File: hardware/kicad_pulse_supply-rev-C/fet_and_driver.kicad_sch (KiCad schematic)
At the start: 52 parts, among them J2 SIG_EXT, Q1 GAN7R0-150LBE, U1 UCC27611DRVT, U4 MAX4378, U6 MCP1703T-5002E/MB

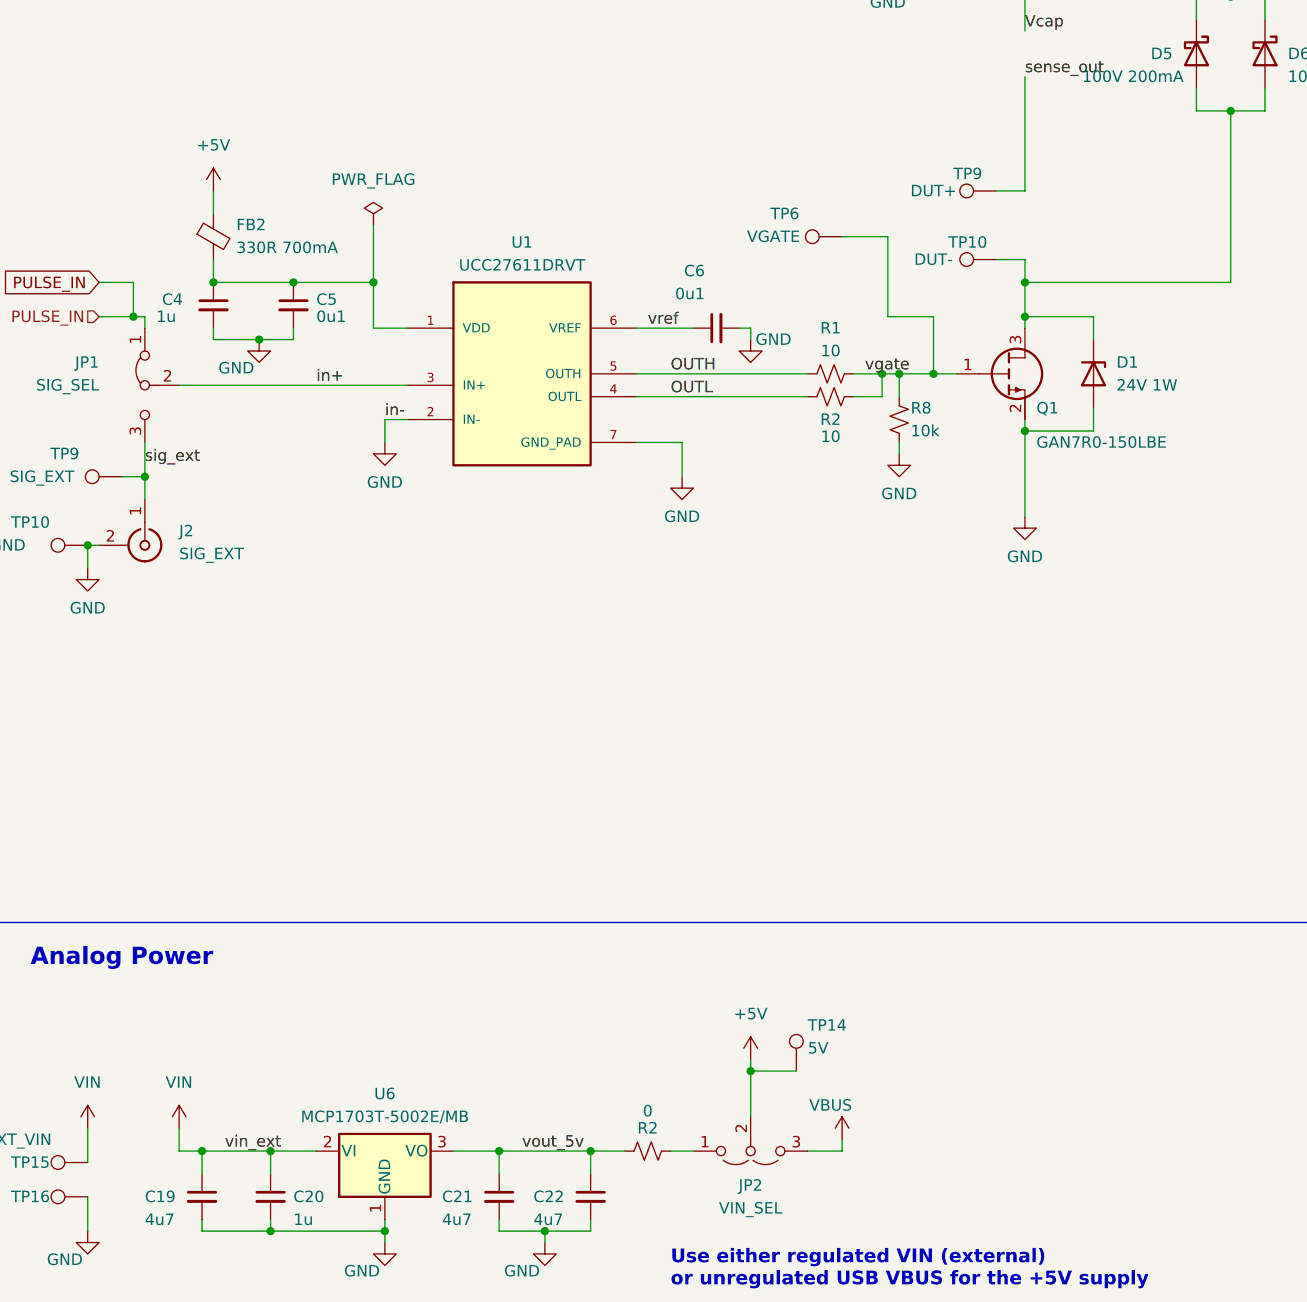
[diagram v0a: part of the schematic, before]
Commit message: Refactored main loop to use Arduino Strings
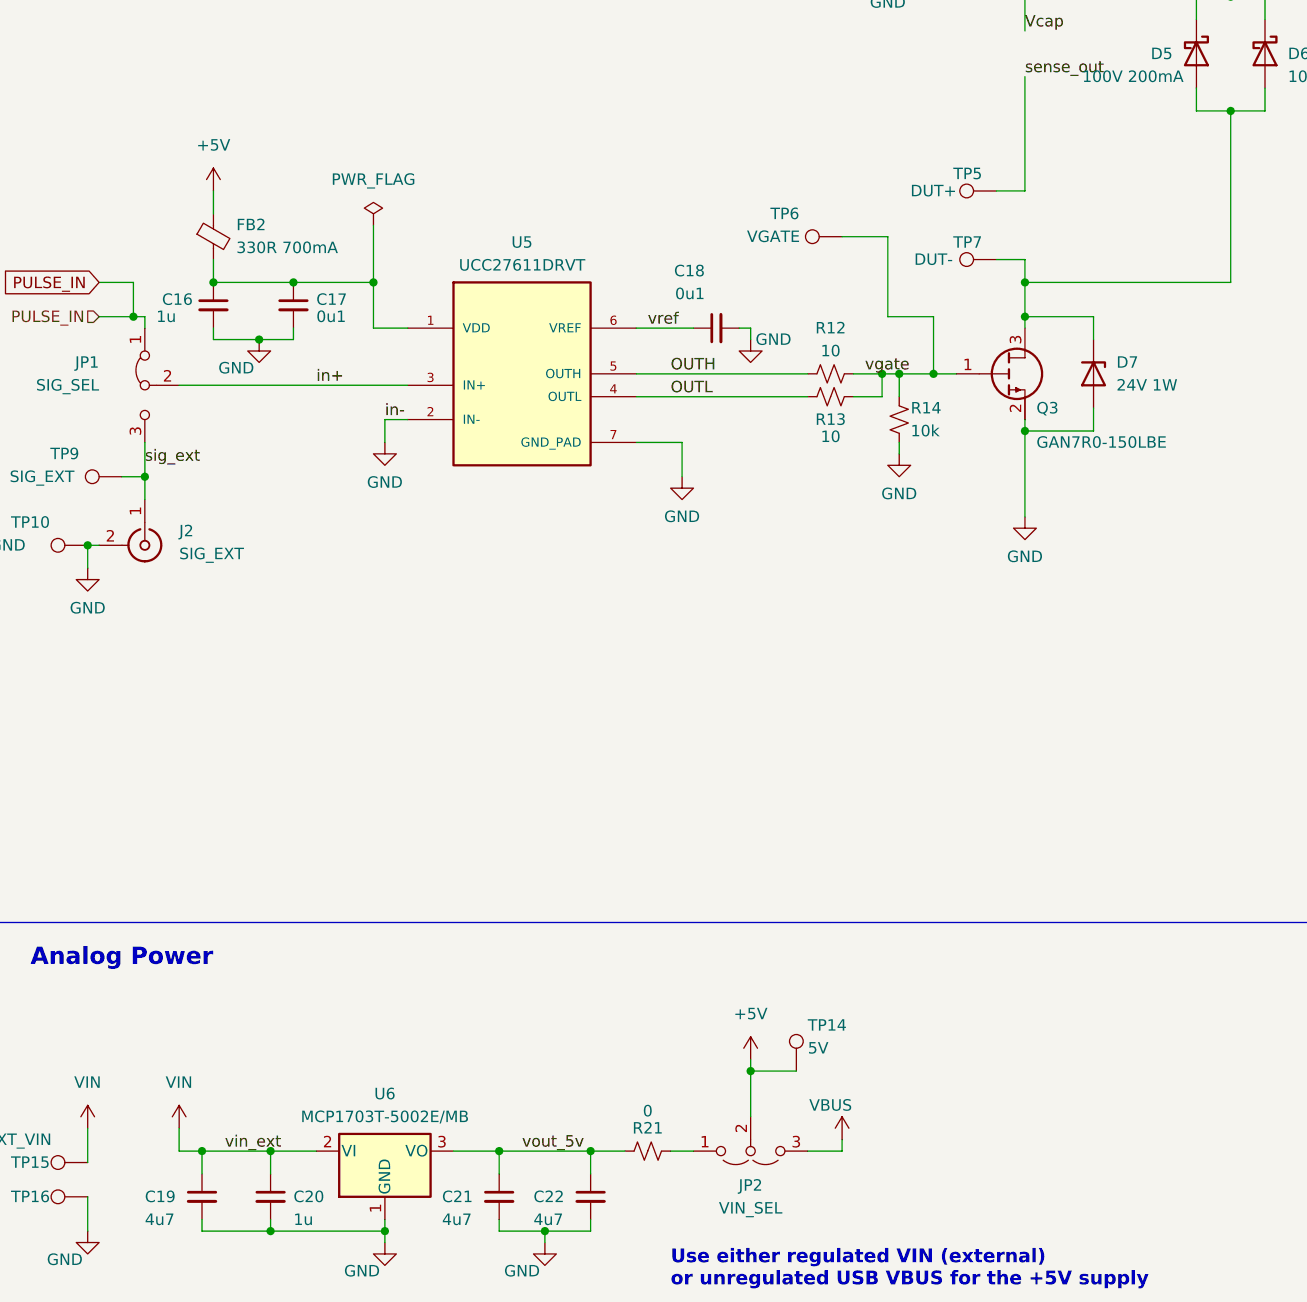
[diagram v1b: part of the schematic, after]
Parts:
- renumbered C4 to C16, C5 to C17, C6 to C18, D1 to D7, Q1 to Q3, R1 to R12, R2 to R13, R8 to R14, R2 to R21, TP9 to TP5, TP10 to TP7, U1 to U5
